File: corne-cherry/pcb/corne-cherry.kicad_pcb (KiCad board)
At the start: 2 copper layers, 275.5 x 105.6 mm, 172 parts, among them J1 MJ-4PP-9, J2 OLED, J3 MJ-4PP-9, J4 OLED, SW1 SW_PUSH, SW10 SW_PUSH, SW11 SW_PUSH, SW12 SW_PUSH, SW13 SW_PUSH, SW14 SW_PUSH, SW15 SW_PUSH, SW16 SW_PUSH, SW17 SW_PUSH, SW18 SW_PUSH, SW19 SW_PUSH, SW2 SW_PUSH, SW20 SW_PUSH, SW21 SW_PUSH, SW22 SW_PUSH, SW23 SW_PUSH, SW24 SW_PUSH, SW25 SW_PUSH, SW26 SW_PUSH, SW27 SW_PUSH, SW28 SW_PUSH, SW29 SW_PUSH, SW3 SW_PUSH, SW30 SW_PUSH, SW31 SW_PUSH, SW32 SW_PUSH, SW33 SW_PUSH, SW34 SW_PUSH, SW35 SW_PUSH, SW36 SW_PUSH, SW37 SW_PUSH, SW38 SW_PUSH, SW39 SW_PUSH, SW4 SW_PUSH, SW40 SW_PUSH, SW41 SW_PUSH, SW42 SW_PUSH, SW5 SW_PUSH, SW6 SW_PUSH, SW7 SW_PUSH, SW8 SW_PUSH, SW9 SW_PUSH, U1 ProMicro, U2 ProMicro

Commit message: Update right side
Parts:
- moved D22 6.00 mm to (284.2, 41.8)
- moved D23 6.00 mm to (265.2, 41.8)
- moved D28 6.00 mm to (284.2, 60.6)
- moved D29 6.00 mm to (265.2, 60.8)
- moved D34 6.00 mm to (284.2, 79.8)
- moved D35 6.00 mm to (265.2, 79.8)
- moved LED28 6.00 mm to (257.6, 51.3)
- moved LED31 6.00 mm to (257.6, 70.3)
- moved LED34 6.00 mm to (276.6, 46.5)
- moved LED35 6.00 mm to (257.6, 46.5)
- moved LED40 6.00 mm to (276.6, 65.5)
- moved LED41 6.00 mm to (257.6, 65.5)
- moved LED46 6.00 mm to (276.6, 84.5)
- moved LED47 6.00 mm to (257.6, 84.5)
- moved REF** 6.00 mm to (238.7, 89.2)
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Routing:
- net GND: track 638.3 -> 653.6 mm, vias 16 -> 18
- net GNDA: track 617.9 -> 631.0 mm
- net VDD: track 573.1 -> 580.5 mm
- net col1_r: track 150.7 -> 155.8 mm
- net Net-(LED31-Pad2): track 71.8 -> 76.7 mm
- net Net-(LED47-Pad4): track 16.6 -> 20.2 mm
- net col0_r: track 175.8 -> 179.2 mm
- net Net-(LED28-Pad4): track 35.9 -> 38.4 mm
- net VCC: track 551.7 -> 553.0 mm
- net col0: track 172.8 -> 174.1 mm
- net col1: track 151.9 -> 153.1 mm
- net row1_r: track 166.9 -> 168.0 mm
- net row2_r: track 172.6 -> 173.7 mm
- net Net-(LED4-Pad2): track 48.1 -> 47.3 mm
- net row0_r: track 184.4 -> 184.9 mm
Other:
- outline, holes or cut-outs redrawn
- board text added: "Corne Cherry Extreme v3.0.1 PCB Designed by foostan Mod by buztard"
- board text added: "JLCJLCJLCJLC"
- board text removed: "Corne Cherry v3.0.1 PCB Designed by foostan"

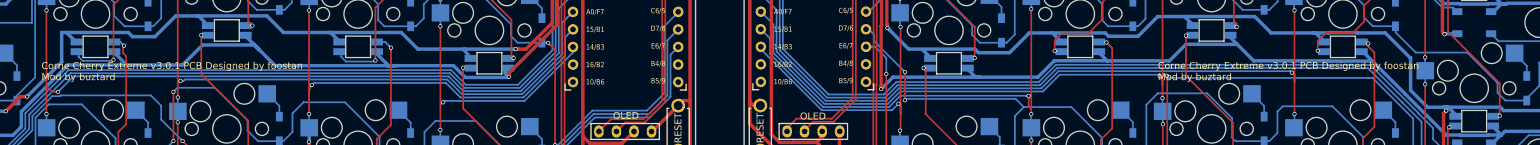
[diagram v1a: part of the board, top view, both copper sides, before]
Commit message: Modify silk
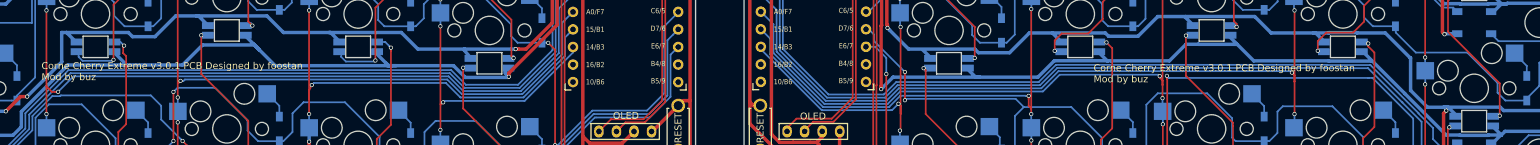
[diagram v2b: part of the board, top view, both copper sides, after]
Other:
- board text added: "Corne Cherry Extreme v3.0.1 PCB Designed by foostan Mod by buz"
- board text removed: "Corne Cherry Extreme v3.0.1 PCB Designed by foostan Mod by buztard"
